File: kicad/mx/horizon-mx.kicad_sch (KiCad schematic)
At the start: 116 parts

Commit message: Update projects to KiCad 6 and regenerate gerbers
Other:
- title: Horizon Choc -> Horizon MX

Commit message: Upgrade revision to 2.3. Remove KiCad 5 files
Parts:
- BTN1: value (none) -> RESET; footprint (none) -> horizon-footprints:SW_Push_6mm
- D1, D10, D11, D12, D13, D14, D15, D16, D17, D18, D19, D2, D20, D21, D22, D23, D24, D25, D26, D27, D28, D29, D3, D30, D31, D32, D33, D34, D35, D36, D37, D38, D39, D4, D40, D41, D42, D43, D44, D45, D46, D47, D48, D49, D5, D50, D51, D52, D6, D7, D8, D9: value (none) -> D; footprint (none) -> horizon-footprints:D_SOD-123
- H1, H2, H3, H4, H5, H6, H7, H8: value (none) -> Hole_Pad; footprint (none) -> horizon-footprints:Mount_M2
- LOGO1: value (none) -> Logo-Bottom; footprint (none) -> horizon-footprints:Logo_Horizon_Small
- LOGO2: value (none) -> Logo-Top; footprint (none) -> horizon-footprints:Logo_Horizon_H
- SW1, SW10, SW11, SW12, SW13, SW14, SW15, SW16, SW17, SW18, SW19, SW2, SW20, SW21, SW22, SW23, SW24, SW25, SW26, SW27, SW28, SW29, SW3, SW30, SW31, SW32, SW33, SW34, SW35, SW36, SW37, SW38, SW39, SW4, SW40, SW41, SW42, SW43, SW44, SW45, SW46, SW47, SW48, SW49, SW5, SW50, SW51, SW52, SW6, SW7, SW8, SW9: value (none) -> SW_Push; footprint (none) -> horizon-footprints:SW_MX
- U1: value (none) -> PRO-MICRO; footprint (none) -> horizon-footprints:Pro-Micro

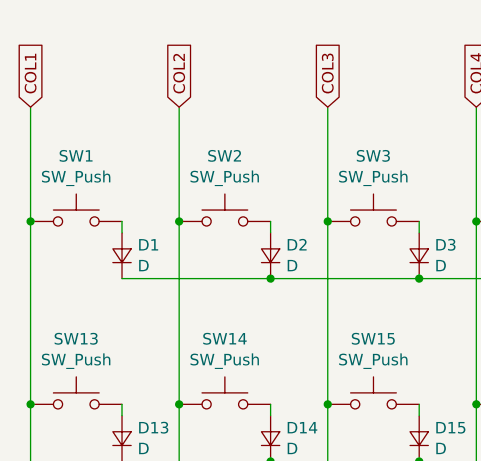
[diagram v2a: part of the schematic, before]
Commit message: Use KiCad 6 symbol library format
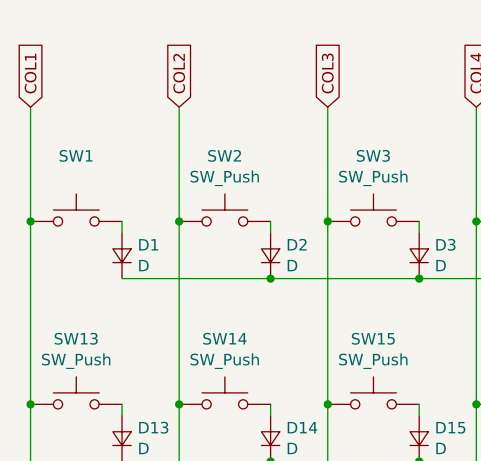
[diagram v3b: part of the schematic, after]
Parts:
- SW1: value SW_Push -> (none); footprint horizon-footprints:SW_MX -> (none)
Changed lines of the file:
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@@
     (in_bom yes) (on_board yes)
     (property "Reference" "SW1" (id 0) (at 25.4 32.131 0))
-    (property "Value" "SW_Push" (id 1) (at 25.4 34.4424 0))
-    (property "Footprint" "horizon-footprints:SW_MX" (id 2) (at 25.4 34.29 0)
+    (property "Value" "" (id 1) (at 25.4 34.4424 0))
+    (property "Footprint" "" (id 2) (at 25.4 34.29 0)
       (effects (font (size 1.27 1.27)) hide)
     )

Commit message: Upgrade plugin and project files to KiCad 7
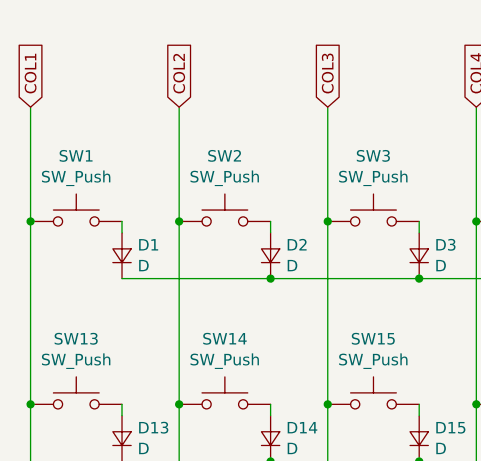
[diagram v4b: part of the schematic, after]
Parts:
- SW1: value (none) -> SW_Push; footprint (none) -> horizon-footprints:SW_MX
